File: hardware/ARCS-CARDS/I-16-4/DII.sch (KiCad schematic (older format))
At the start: 40 parts

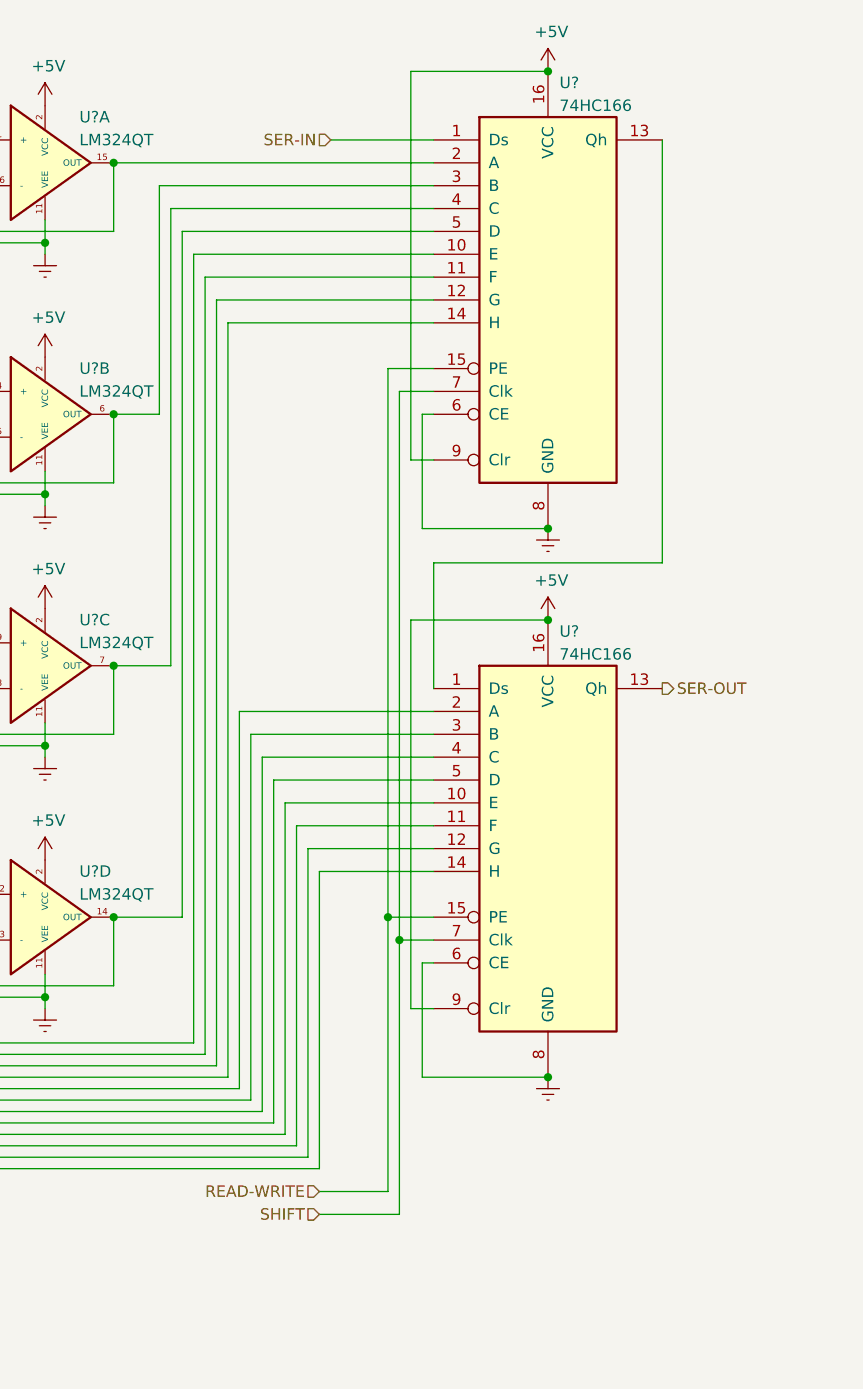
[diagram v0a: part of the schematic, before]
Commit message: Create analog input interface card.
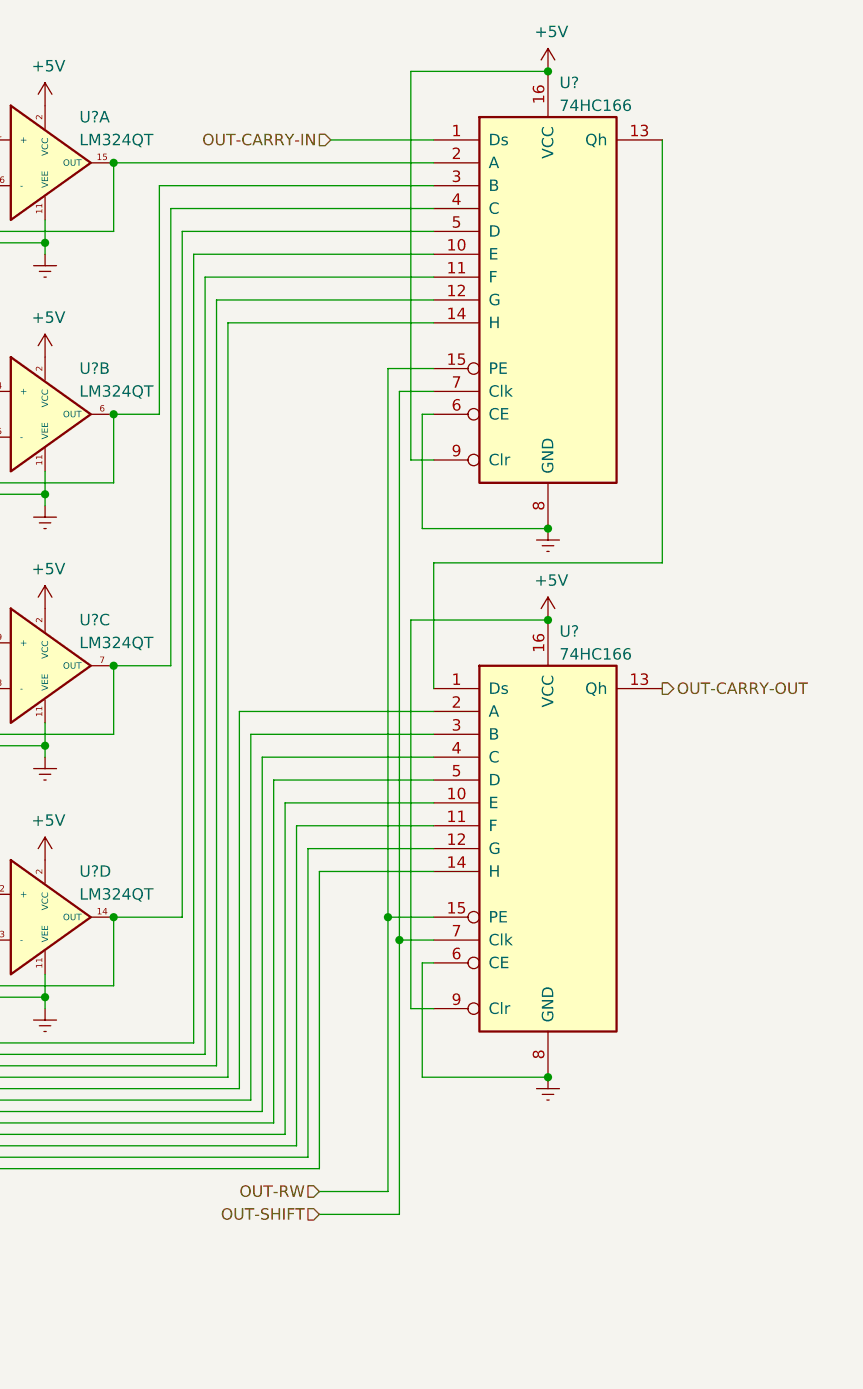
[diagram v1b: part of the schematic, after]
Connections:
- net READ-WRITE renamed OUT-RW
- net SER-IN renamed OUT-CARRY-IN
- net SER-OUT renamed OUT-CARRY-OUT
- net SHIFT renamed OUT-SHIFT
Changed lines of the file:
@@
 	9100 4650 8600 4650
 Text HLabel 8650 1450 0    50   Input ~ 0
-SER-IN
+OUT-CARRY-IN
 Wire Wire Line
 	8650 1450 9100 1450
 Text HLabel 10100 3850 2    50   Output ~ 0
-SER-OUT
+OUT-CARRY-OUT
 Text HLabel 8600 6150 0    50   Input ~ 0
-SHIFT
+OUT-SHIFT
 Text HLabel 8600 6050 0    50   Input ~ 0
-READ-WRITE
+OUT-RW
 Connection ~ 8950 4950
 Connection ~ 8900 4850

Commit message: Create analog input interface card.
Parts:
- U? (x16): symbol OPAmps:LM324QT -> ARCS-CARDS-I-16-4-rescue:LM324QT-OPAmps
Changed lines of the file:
@@
 	8900 2450 9100 2450
 $Comp
-L OPAmps:LM324QT U?
+L ARCS-CARDS-I-16-4-rescue:LM324QT-OPAmps U?
 U 1 1 5CA49C17
 P 7400 1550
@@
 $EndComp
 $Comp
-L OPAmps:LM324QT U?
+L ARCS-CARDS-I-16-4-rescue:LM324QT-OPAmps U?
 U 2 1 5CA49C1E
 P 7400 2650
@@
 $EndComp
 $Comp
-L OPAmps:LM324QT U?
+L ARCS-CARDS-I-16-4-rescue:LM324QT-OPAmps U?
 U 3 1 5CA49C25
 P 7400 3750
@@
 $EndComp
 $Comp
-L OPAmps:LM324QT U?
+L ARCS-CARDS-I-16-4-rescue:LM324QT-OPAmps U?
 U 4 1 5CA49C2C
 P 7400 4850
@@
 	6450 4750 6850 4750
 $Comp
-L OPAmps:LM324QT U?
+L ARCS-CARDS-I-16-4-rescue:LM324QT-OPAmps U?
 U 1 1 5CA80C64
 P 5700 1550
@@
 $EndComp
 $Comp
-L OPAmps:LM324QT U?
+L ARCS-CARDS-I-16-4-rescue:LM324QT-OPAmps U?
 U 2 1 5CA80C6B
 P 5700 2650
@@
 $EndComp
 $Comp
-L OPAmps:LM324QT U?
+L ARCS-CARDS-I-16-4-rescue:LM324QT-OPAmps U?
 U 3 1 5CA80C72
 P 5700 3750
@@
 $EndComp
 $Comp
-L OPAmps:LM324QT U?
+L ARCS-CARDS-I-16-4-rescue:LM324QT-OPAmps U?
 U 4 1 5CA80C79
 P 5700 4850
@@
 	4750 4750 5150 4750
 $Comp
-L OPAmps:LM324QT U?
+L ARCS-CARDS-I-16-4-rescue:LM324QT-OPAmps U?
 U 1 1 5CA86B08
 P 4000 1550
@@
 $EndComp
 $Comp
-L OPAmps:LM324QT U?
+L ARCS-CARDS-I-16-4-rescue:LM324QT-OPAmps U?
 U 2 1 5CA86B0F
 P 4000 2650
@@
 $EndComp
 $Comp
-L OPAmps:LM324QT U?
+L ARCS-CARDS-I-16-4-rescue:LM324QT-OPAmps U?
 U 3 1 5CA86B16
 P 4000 3750
@@
 $EndComp
 $Comp
-L OPAmps:LM324QT U?
+L ARCS-CARDS-I-16-4-rescue:LM324QT-OPAmps U?
 U 4 1 5CA86B1D
 P 4000 4850
@@
 	3050 4750 3450 4750
 $Comp
-L OPAmps:LM324QT U?
+L ARCS-CARDS-I-16-4-rescue:LM324QT-OPAmps U?
 U 1 1 5CA86BB4
 P 2300 1550
@@
 $EndComp
 $Comp
-L OPAmps:LM324QT U?
+L ARCS-CARDS-I-16-4-rescue:LM324QT-OPAmps U?
 U 2 1 5CA86BBB
 P 2300 2650
@@
 $EndComp
 $Comp
-L OPAmps:LM324QT U?
+L ARCS-CARDS-I-16-4-rescue:LM324QT-OPAmps U?
 U 3 1 5CA86BC2
 P 2300 3750
@@
 $EndComp
 $Comp
-L OPAmps:LM324QT U?
+L ARCS-CARDS-I-16-4-rescue:LM324QT-OPAmps U?
 U 4 1 5CA86BC9
 P 2300 4850
